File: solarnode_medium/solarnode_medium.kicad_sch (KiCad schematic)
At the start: 8 parts, among them SW1 3*4*2mm

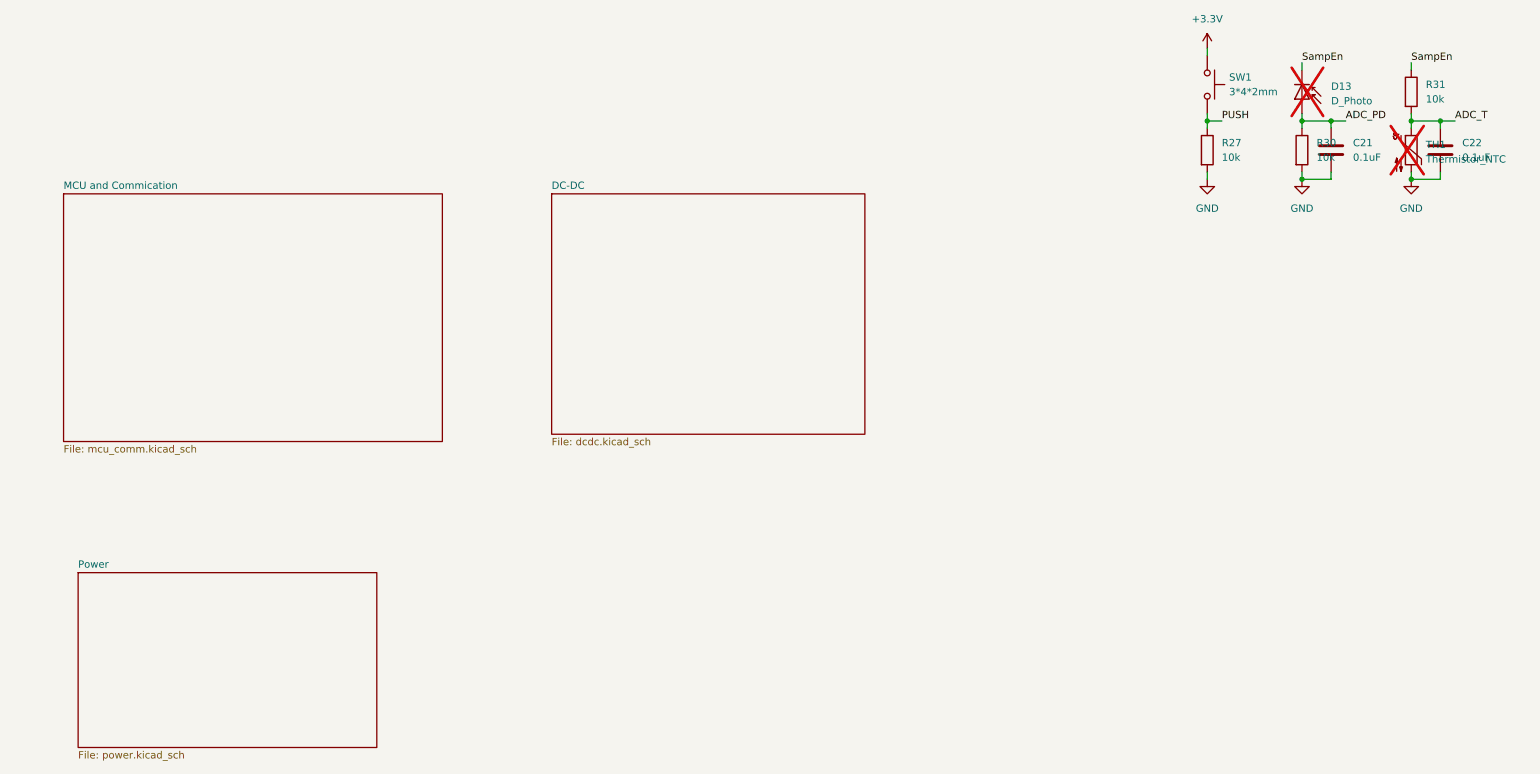
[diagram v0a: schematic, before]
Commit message: 修改原理图，添加子原理图间连接，添加MCU和一些外围电路
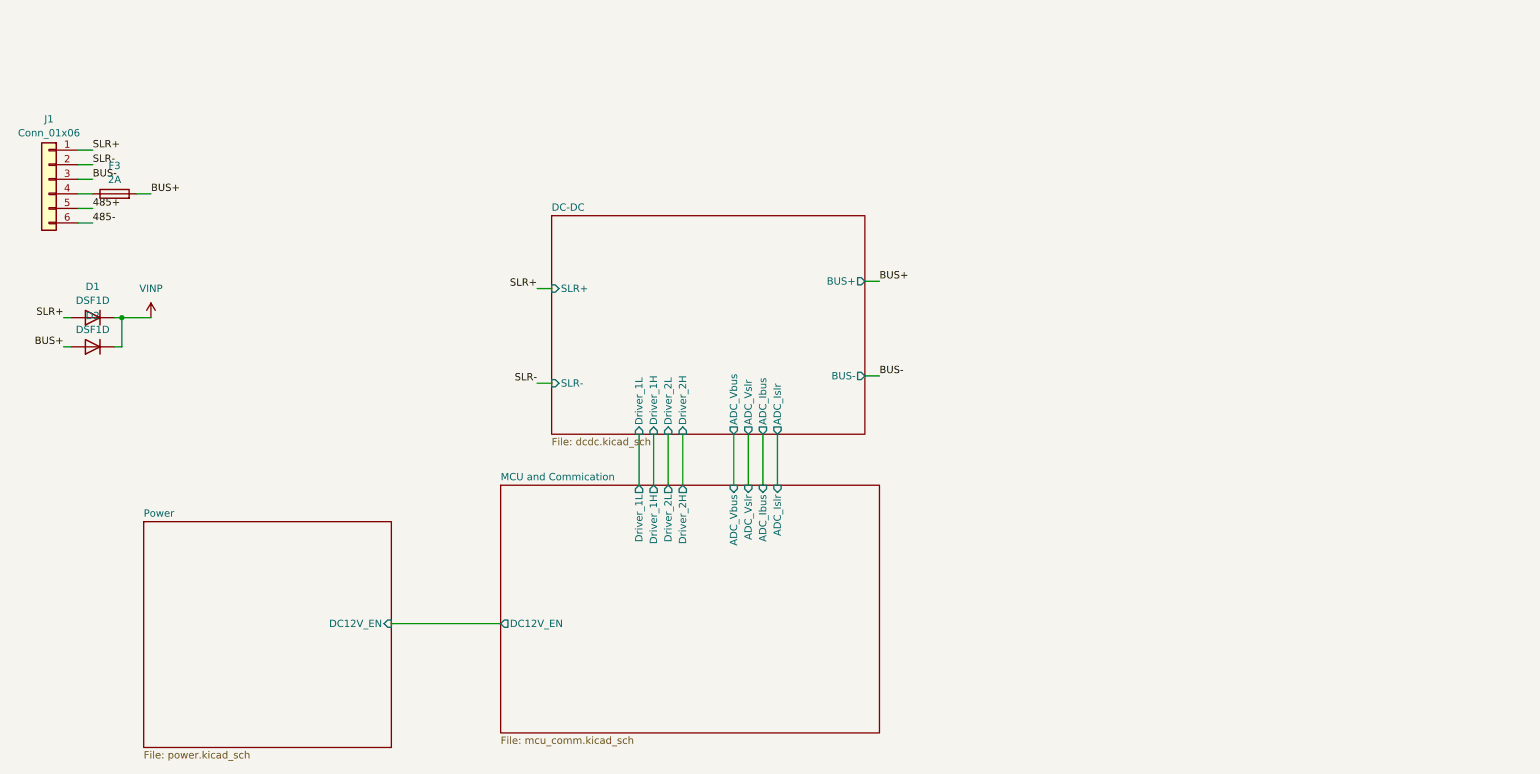
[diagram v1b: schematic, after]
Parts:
- removed C21, C22: 0.1uF, Capacitor_SMD:C_0402_1005Metric, symbol Device:C
- removed D13: D_Photo, Diode_SMD:D_0805_2012Metric, symbol Device:D_Photo
- removed R27, R30, R31: 10k, Resistor_SMD:R_0402_1005Metric, symbol Device:R
- removed SW1: 3*4*2mm, Button_Switch_SMD:SW_Push_SPST_NO_Alps_SKRK, symbol Switch:SW_Push
- removed TH1: Thermistor_NTC, Resistor_SMD:R_0805_2012Metric, symbol Device:Thermistor_NTC
- added D1, D2: DSF1D, Diode_SMD:D_SOD-123F, symbol Device:D
- added F3: 2A, Fuse:Fuse_1206_3216Metric, symbol Device:Fuse
- added J1: Conn_01x06, TerminalBlock:TerminalBlock_bornier-6_P5.08mm, symbol Connector_Generic:Conn_01x06
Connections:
- new net: F3.1, J1.4 (Pin_4)
- new net 485+: J1.5 (Pin_5)
- new net 485-: J1.6 (Pin_6)
- new net BUS+: D2.2 (A), F3.2
- new net BUS-: J1.3 (Pin_3)
- new net SLR+: D1.2 (A), J1.1 (Pin_1)
- new net SLR-: J1.2 (Pin_2)
- new net VINP: D1.1 (K), D2.1 (K)
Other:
- sheet DC-DC ports: added ADC_Ibus, ADC_Islr, ADC_Vbus, ADC_Vslr, BUS+, BUS-, Driver_1H, Driver_1L, Driver_2H, Driver_2L, SLR+, SLR-; removed none
- sheet MCU and Commication ports: added ADC_Ibus, ADC_Islr, ADC_Vbus, ADC_Vslr, DC12V_EN, Driver_1H, Driver_1L, Driver_2H, Driver_2L; removed none
- sheet Power ports: added DC12V_EN; removed none

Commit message: 添加断线报警器探测线接口
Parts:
- added J3: Conn_01x02, Connector_PinHeader_2.54mm:PinHeader_1x02_P2.54mm_Vertical, symbol Connector_Generic:Conn_01x02
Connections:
- new net MCU and Commication/DET_LINE1: J3.1 (Pin_1)
- new net MCU and Commication/DET_LINE2: J3.2 (Pin_2)
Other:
- sheet MCU and Commication ports: added DET_LINE1, DET_LINE2; removed none
- note added: "断线报警器探测线"
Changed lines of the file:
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@@
+	(wire
+		(pts
+			(xy 170.18 123.19) (xy 172.72 123.19)
+		)
+		(stroke
+			(width 0)
+			(type default)
+		)
+	)
 	(wire
 		(pts
@@
 	(wire
 		(pts
+			(xy 170.18 125.73) (xy 172.72 125.73)
+		)
+		(stroke
+			(width 0)
+			(type default)
+		)
+	)
+	(wire
+		(pts
 			(xy 33.02 44.45) (xy 30.48 44.45)
 		)
@@
 			(width 0)
 			(type default)
+		)
+	)
+	(text "断线报警器探测线"
+		(exclude_from_sim no)
+		(at 183.642 129.54 0)
+		(effects
+			(font
+				(size 1.27 1.27)
+			)
 		)
 	)
@@
 		)
 	)
+	(symbol
+		(lib_id "Connector_Generic:Conn_01x02")
+		(at 177.8 123.19 0)
+		(unit 1)
+		(exclude_from_sim no)
+		(in_bom yes)
+		(on_board yes)
+		(dnp no)
+		(fields_autoplaced yes)
+		(property "Reference" "J3"
+			(at 180.34 123.1899 0)
+			(effects
+				(font
+					(size 1.27 1.27)
+				)
+				(justify left)
+			)
+		)
+		(property "Value" "Conn_01x02"
+			(at 180.34 125.7299 0)
+			(effects
+				(font
+					(size 1.27 1.27)
+				)
+				(justify left)
+			)
+		)
+		(property "Footprint" "Connector_PinHeader_2.54mm:PinHeader_1x02_P2.54mm_Vertical"
+			(at 177.8 123.19 0)
+			(effects
+				(font
+					(size 1.27 1.27)
+				)
+				(hide yes)
+			)
+		)
+		(property "Datasheet" "~"
+			(at 177.8 123.19 0)
+			(effects
+				(font
+					(size 1.27 1.27)
+				)
+				(hide yes)
+			)
+		)
+		(property "Description" "Generic connector, single row, 01x02, script generated (kicad-library-utils/schlib/autogen/connector/)"
+			(at 177.8 123.19 0)
+			(effects
+				(font
+					(size 1.27 1.27)
+				)
+				(hide yes)
+			)
+		)
+		(pin "1"
+		)
+		(pin "2"
+		)
+		(instances
+			(project ""
+				(path "/02bd9ea1-7d62-409c-9b7f-8139c011cbf3"
+					(reference "J3")
+					(unit 1)
+				)
+			)
+		)
+	)
 	(sheet
 		(at 104.14 102.87)
@@
 			)
 		)
+		(pin "DET_LINE1" bidirectional
+			(at 170.18 123.19 0)
+			(effects
+				(font
+					(size 1.27 1.27)
+				)
+				(justify right)
+			)
+		)
+		(pin "DET_LINE2" bidirectional
+			(at 170.18 125.73 0)
+			(effects
+				(font
+					(size 1.27 1.27)
+				)
+				(justify right)
+			)
+		)
